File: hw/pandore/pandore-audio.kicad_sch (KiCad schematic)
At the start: 1 part, among them U9 Teensy 4.1

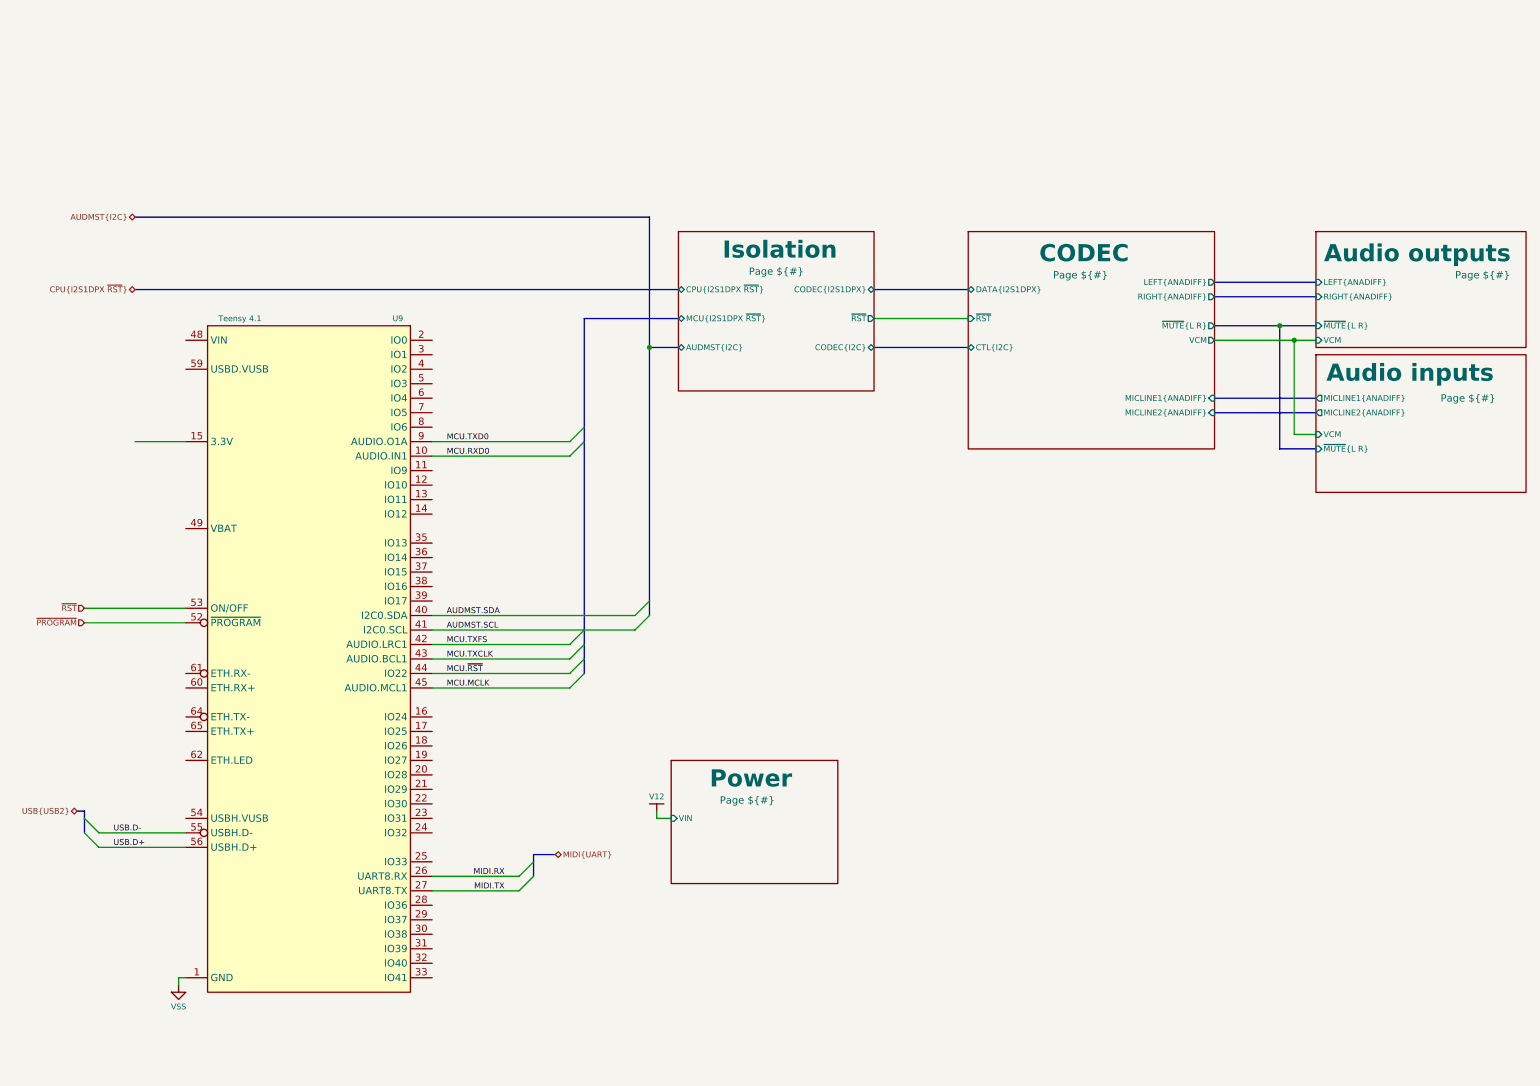
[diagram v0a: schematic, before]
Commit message: most of board control signals added, routed and defined
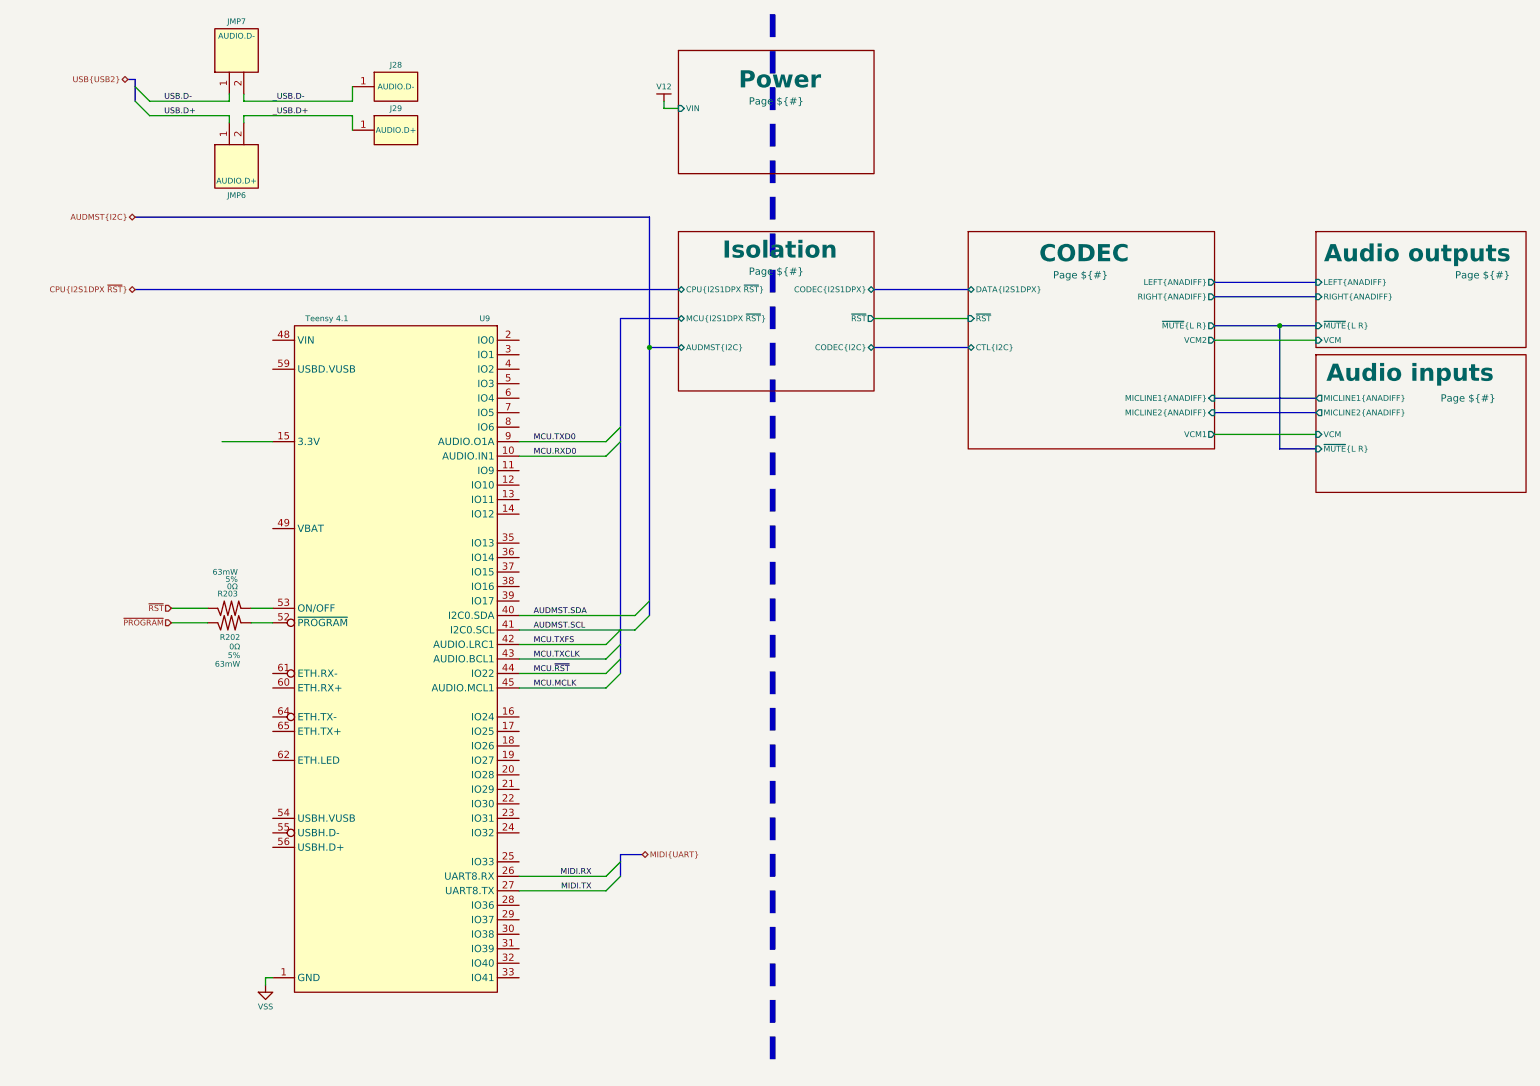
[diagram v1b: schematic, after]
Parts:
- added J28: AUDIO.D-, footprint, symbol reekilib_con:hdr-1x1
- added J29: AUDIO.D+, footprint, symbol reekilib_con:hdr-1x1
- added JMP6: AUDIO.D+, reekilib_con:HDR254P1X02-TH, symbol reekilib_con:hdr-1x2
- added JMP7: AUDIO.D-, reekilib_con:HDR254P1X02-TH, symbol reekilib_con:hdr-1x2
- added R202, R203: ${Resistance}, ${Tolerance}, ${Power}, reekilib_res:RESC1005, symbol reekilib_res:res
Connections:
- net USB.D+: now also JMP6.1; no longer U9.56 (USBH.D+)
- net USB.D-: now also JMP7.1; no longer U9.55 (USBH.D-)
- net ~{PROGRAM}: now also R202.2; no longer U9.52 (~{PROGRAM})
- net ~{RST}: now also R203.2; no longer U9.53 (ON/OFF)
- new net: R202.1, U9.52 (~{PROGRAM})
- new net: R203.1, U9.53 (ON/OFF)
- new net _USB.D+: J29.1, JMP6.2
- new net _USB.D-: J28.1, JMP7.2
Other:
- sheet CODEC ports: added VCM1, VCM2; removed VCM
- moved on the sheet: U9

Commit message: added expansion port and more ctl to rp2350s routing much progress
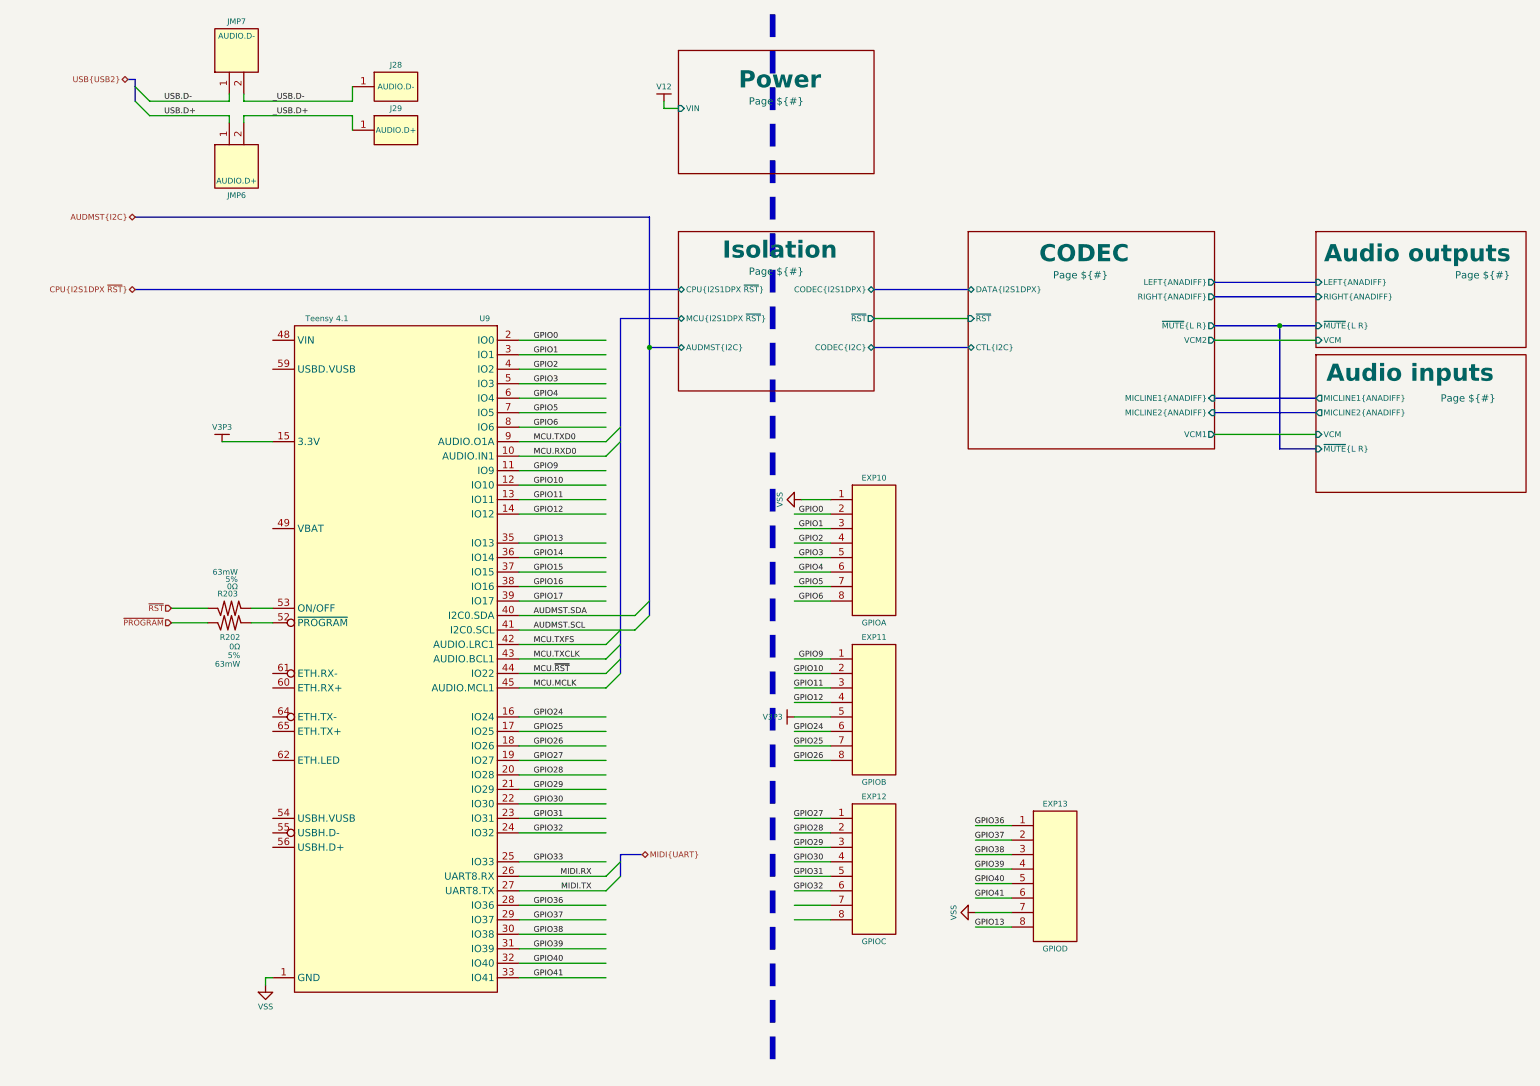
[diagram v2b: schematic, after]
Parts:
- added EXP10: GPIOA, reekilib_con:HDR254P1X08-TH, symbol reekilib_con:hdr-1x8
- added EXP11: GPIOB, reekilib_con:HDR254P1X08-TH, symbol reekilib_con:hdr-1x8
- added EXP12: GPIOC, reekilib_con:HDR254P1X08-TH, symbol reekilib_con:hdr-1x8
- added EXP13: GPIOD, reekilib_con:HDR254P1X08-TH, symbol reekilib_con:hdr-1x8
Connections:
- net VSS: now also EXP10.1, EXP13.7
- net GPIO9: now reaches U9.11 (IO9)
- net GPIO9: now also EXP11.1
- net GPIO10: now reaches U9.12 (IO10)
- net GPIO10: now also EXP11.2
- net GPIO11: now reaches U9.13 (IO11)
- net GPIO11: now also EXP11.3
- net GPIO12: now reaches U9.14 (IO12)
- net GPIO12: now also EXP11.4
- net V3P3: now reaches U9.15 (3.3V), U9.46 (3.3V), U9.50 (3.3V)
- net V3P3: now also EXP11.5
- net GPIO24: now reaches U9.16 (IO24)
- net GPIO24: now also EXP11.6
- net GPIO25: now reaches U9.17 (IO25)
- net GPIO25: now also EXP11.7
- net GPIO26: now reaches U9.18 (IO26)
- net GPIO26: now also EXP11.8
- net GPIO27: now reaches U9.19 (IO27)
- net GPIO27: now also EXP12.1
- net GPIO0: now reaches U9.2 (IO0)
- net GPIO0: now also EXP10.2
- net GPIO28: now reaches U9.20 (IO28)
- net GPIO28: now also EXP12.2
- net GPIO29: now reaches U9.21 (IO29)
- net GPIO29: now also EXP12.3
- net GPIO30: now reaches U9.22 (IO30)
- net GPIO30: now also EXP12.4
- net GPIO31: now reaches U9.23 (IO31)
- net GPIO31: now also EXP12.5
- net GPIO32: now reaches U9.24 (IO32)
- net GPIO32: now also EXP12.6
- net GPIO33: now reaches U9.25 (IO33)
- net GPIO36: now reaches U9.28 (IO36)
- net GPIO36: now also EXP13.1
- net GPIO37: now reaches U9.29 (IO37)
- net GPIO37: now also EXP13.2
- net GPIO1: now reaches U9.3 (IO1)
- net GPIO1: now also EXP10.3
- net GPIO38: now reaches U9.30 (IO38)
- net GPIO38: now also EXP13.3
- net GPIO39: now reaches U9.31 (IO39)
- net GPIO39: now also EXP13.4
- net GPIO40: now reaches U9.32 (IO40)
- net GPIO40: now also EXP13.5
- net GPIO41: now reaches U9.33 (IO41)
- net GPIO41: now also EXP13.6
- net GPIO13: now reaches U9.35 (IO13)
- net GPIO13: now also EXP13.8
- net GPIO14: now reaches U9.36 (IO14)
- net GPIO15: now reaches U9.37 (IO15)
- net GPIO16: now reaches U9.38 (IO16)
- net GPIO17: now reaches U9.39 (IO17)
- net GPIO2: now reaches U9.4 (IO2)
- net GPIO2: now also EXP10.4
- net GPIO3: now reaches U9.5 (IO3)
- net GPIO3: now also EXP10.5
- net GPIO4: now reaches U9.6 (IO4)
- net GPIO4: now also EXP10.6
- net GPIO5: now reaches U9.7 (IO5)
- net GPIO5: now also EXP10.7
- net GPIO6: now reaches U9.8 (IO6)
- net GPIO6: now also EXP10.8

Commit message: more routing/placement done added 5v load switch 1A each added second fan circuit redone all diffpair routing following new stackup calc added all (?) missing connectors to unused pins
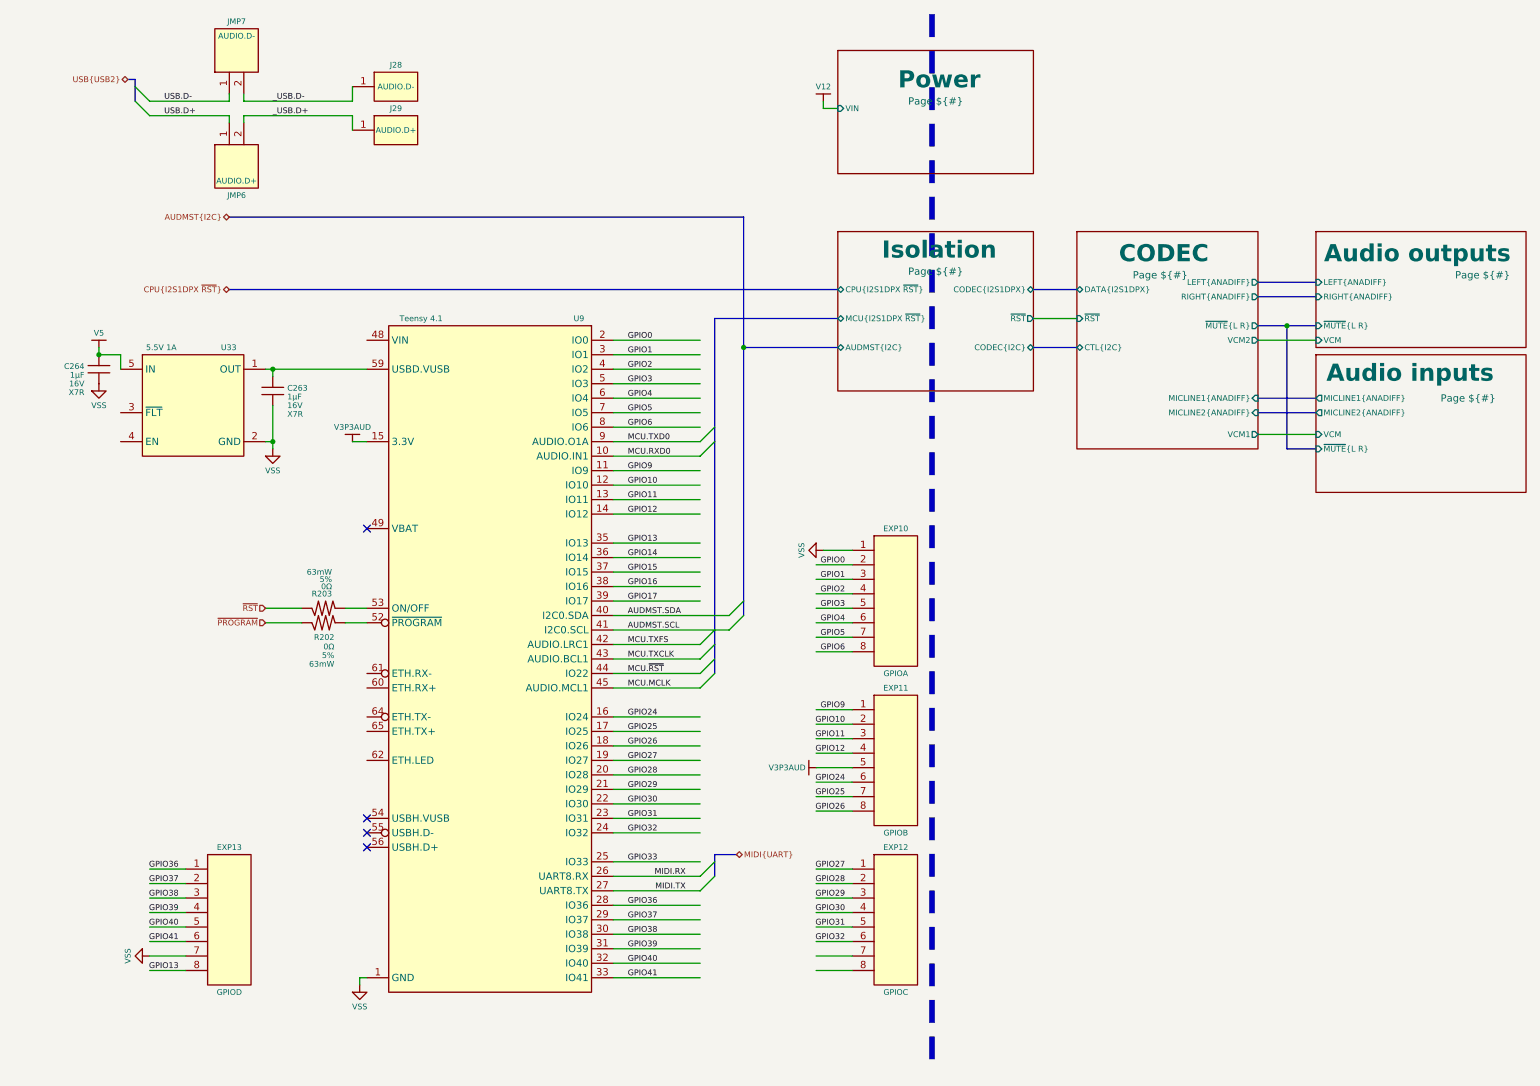
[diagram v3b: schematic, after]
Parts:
- added C263, C264: ${Capacitance}, ${Voltage}, ${Dielectric}, reekilib_cap:CAPC1608, symbol reekilib_cap:cap
- added U33: 5.5V 1A, reekilib_sot:SOT95P280X100-5, symbol reekilib_psw:ET2016x
- J28, J29: footprint footprint -> reekilib_con:samesky_CPG-23; Link (none) -> https://www.sameskydevices.com/product/interconnect/connect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; MFG (none) -> Same Sky (Formerly CUI Devices); MPN (none) -> CPG-23-SMT-TR
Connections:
- net VSS: now also C263.1, C264.1, U33.2 (GND)
- net at U9.59 (USBD.VUSB): now also C263.2, U33.1 (OUT)
- net V3P3 renamed V3P3AUD
- new net V5: C264.2, U33.5 (IN)
- no-connect marks 0 -> 4
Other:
- moved on the sheet: EXP10, EXP11, EXP12, EXP13, R202, R203, U9

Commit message: last sprint almost done, most routing done
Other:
- sheet Audio outputs ports: added VCMMON; removed none
- sheet CODEC ports: added VCM0; removed none
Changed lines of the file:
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@@
 		)
 	)
+	(wire
+		(pts
+			(xy 228.6 64.77) (xy 238.76 64.77)
+		)
+		(stroke
+			(width 0)
+			(type default)
+		)
+	)
 	(bus
 		(pts
@@
 			)
 		)
+		(pin "VCMMON" input
+			(at 238.76 64.77 180)
+			(effects
+				(font
+					(size 1.016 1.016)
+				)
+				(justify left)
+			)
+		)
 		(instances
 			(project "pandore"
@@
 			(effects
 				(font
+					(size 1.016 1.016)
+				)
+				(justify right)
+			)
+		)
+		(pin "VCM0" output
+			(at 228.6 64.77 0)
+			(effects
+				(font

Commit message: all routed, review starting
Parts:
- added R281: ${Resistance}, ${Tolerance}, ${Power}, reekilib_res:RESC1005, symbol reekilib_res:res
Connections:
- net EN: now reaches U33.4 (EN)
- net EN: now also R281.1
- new net V3P3: R281.2
